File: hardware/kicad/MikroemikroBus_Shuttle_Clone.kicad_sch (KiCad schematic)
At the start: 3 parts, among them U28 X1270WV-2X08B-6TV01

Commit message: updating symbols to use kicad footprints where possible
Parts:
- C18, C19: footprint 5v rail sm-easyedapro:C0603 -> Capacitor_SMD:C_0603_1608Metric
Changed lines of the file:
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@@
 			)
 		)
-		(property "Footprint" "5v rail sm-easyedapro:C0603"
+		(property "Footprint" "Capacitor_SMD:C_0603_1608Metric"
 			(at 162.56 93.98 0)
 			(effects
@@
 			)
 		)
-		(property "Footprint" "5v rail sm-easyedapro:C0603"
+		(property "Footprint" "Capacitor_SMD:C_0603_1608Metric"
 			(at 107.95 93.98 0)
 			(effects

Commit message: update
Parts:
- renumbered C18 to C131, C19 to C133, U28 to U83
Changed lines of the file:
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@@
 		(dnp no)
 		(fields_autoplaced yes)
-		(property "Reference" "C19"
+		(property "Reference" "C133"
 			(at 166.37 93.9799 90)
 			(effects
@@
 				(path "/3f85abf4-0b95-4c4a-b7e9-06f59ca1ea3d/5c2e021f-c2d4-49e2-8c36-9a64f1f12001/1974f87f-12b5-4c85-8a00-765c6eb0fd1f"
 					(reference "C133")
-					(unit 1)
-				)
-				(path "/3f85abf4-0b95-4c4a-b7e9-06f59ca1ea3d/5c2e021f-c2d4-49e2-8c36-9a64f1f12001/83efc904-75ae-4d48-8a92-f421069b4636"
-					(reference "C19")
 					(unit 1)
 				)
@@
 		(on_board yes)
 		(dnp no)
-		(property "Reference" "#PWR075"
+		(property "Reference" "#PWR0170"
 			(at 162.56 104.14 0)
 			(effects
@@
 				(path "/3f85abf4-0b95-4c4a-b7e9-06f59ca1ea3d/5c2e021f-c2d4-49e2-8c36-9a64f1f12001/1974f87f-12b5-4c85-8a00-765c6eb0fd1f"
 					(reference "#PWR0170")
-					(unit 1)
-				)
-				(path "/3f85abf4-0b95-4c4a-b7e9-06f59ca1ea3d/5c2e021f-c2d4-49e2-8c36-9a64f1f12001/83efc904-75ae-4d48-8a92-f421069b4636"
-					(reference "#PWR075")
 					(unit 1)
 				)
@@
 		(on_board yes)
 		(dnp no)
-		(property "Reference" "#PWR072"
+		(property "Reference" "#PWR0167"
 			(at 107.95 104.14 0)
 			(effects
@@
 				(path "/3f85abf4-0b95-4c4a-b7e9-06f59ca1ea3d/5c2e021f-c2d4-49e2-8c36-9a64f1f12001/1974f87f-12b5-4c85-8a00-765c6eb0fd1f"
 					(reference "#PWR0167")
-					(unit 1)
-				)
-				(path "/3f85abf4-0b95-4c4a-b7e9-06f59ca1ea3d/5c2e021f-c2d4-49e2-8c36-9a64f1f12001/83efc904-75ae-4d48-8a92-f421069b4636"
-					(reference "#PWR072")
 					(unit 1)
 				)
@@
 		(dnp no)
 		(fields_autoplaced yes)
-		(property "Reference" "C18"
+		(property "Reference" "C131"
 			(at 111.76 93.9799 90)
 			(effects
@@
 				(path "/3f85abf4-0b95-4c4a-b7e9-06f59ca1ea3d/5c2e021f-c2d4-49e2-8c36-9a64f1f12001/1974f87f-12b5-4c85-8a00-765c6eb0fd1f"
 					(reference "C131")
-					(unit 1)
-				)
-				(path "/3f85abf4-0b95-4c4a-b7e9-06f59ca1ea3d/5c2e021f-c2d4-49e2-8c36-9a64f1f12001/83efc904-75ae-4d48-8a92-f421069b4636"
-					(reference "C18")
 					(unit 1)
 				)
@@
 		(on_board yes)
 		(dnp no)
-		(property "Reference" "#PWR074"
+		(property "Reference" "#PWR0169"
 			(at 151.13 106.68 0)
 			(effects
@@
 				(path "/3f85abf4-0b95-4c4a-b7e9-06f59ca1ea3d/5c2e021f-c2d4-49e2-8c36-9a64f1f12001/1974f87f-12b5-4c85-8a00-765c6eb0fd1f"
 					(reference "#PWR0169")
-					(unit 1)
-				)
-				(path "/3f85abf4-0b95-4c4a-b7e9-06f59ca1ea3d/5c2e021f-c2d4-49e2-8c36-9a64f1f12001/83efc904-75ae-4d48-8a92-f421069b4636"
-					(reference "#PWR074")
 					(unit 1)
 				)
@@
 		(on_board yes)
 		(dnp no)
-		(property "Reference" "#PWR073"
+		(property "Reference" "#PWR0168"
 			(at 121.92 104.14 0)
 			(effects
@@
 				(path "/3f85abf4-0b95-4c4a-b7e9-06f59ca1ea3d/5c2e021f-c2d4-49e2-8c36-9a64f1f12001/1974f87f-12b5-4c85-8a00-765c6eb0fd1f"
 					(reference "#PWR0168")
-					(unit 1)
-				)
-				(path "/3f85abf4-0b95-4c4a-b7e9-06f59ca1ea3d/5c2e021f-c2d4-49e2-8c36-9a64f1f12001/83efc904-75ae-4d48-8a92-f421069b4636"
-					(reference "#PWR073")
 					(unit 1)
 				)
@@
 		(on_board yes)
 		(dnp no)
-		(property "Reference" "U28"
+		(property "Reference" "U83"
 			(at 135.89 91.44 0)
 			(effects
@@
 					(unit 1)
 				)
-				(path "/3f85abf4-0b95-4c4a-b7e9-06f59ca1ea3d/5c2e021f-c2d4-49e2-8c36-9a64f1f12001/83efc904-75ae-4d48-8a92-f421069b4636"
-					(reference "U28")
-					(unit 1)
-				)

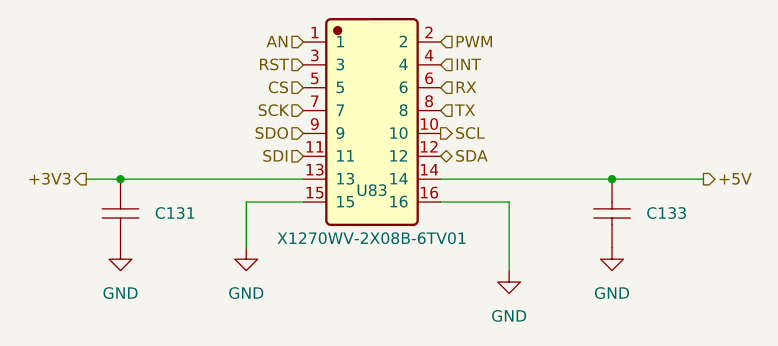
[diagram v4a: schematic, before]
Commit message: fixing inconsistencies in value convention
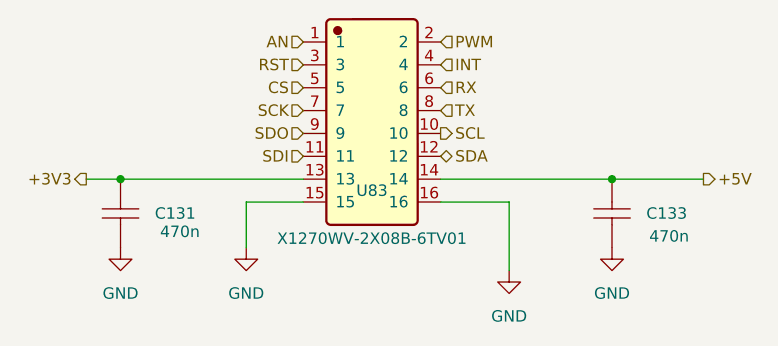
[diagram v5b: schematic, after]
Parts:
- C131, C133: value 470nF -> 470n
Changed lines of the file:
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@@
 		(on_board yes)
 		(dnp no)
-		(fields_autoplaced yes)
 		(property "Reference" "C133"
 			(at 166.37 93.9799 90)
@@
 			)
 		)
-		(property "Value" "470nF"
-			(at 162.56 93.98 0)
-			(effects
-				(font
-					(size 1.27 1.27)
-				)
-				(hide yes)
+		(property "Value" "470n"
+			(at 168.91 96.52 90)
+			(effects
+				(font
+					(size 1.27 1.27)
+				)
 			)
 		)
@@
 		(on_board yes)
 		(dnp no)
-		(fields_autoplaced yes)
 		(property "Reference" "C131"
 			(at 111.76 93.9799 90)
@@
 			)
 		)
-		(property "Value" "470nF"
-			(at 107.95 93.98 0)
-			(effects
-				(font
-					(size 1.27 1.27)
-				)
-				(hide yes)
-			)
-		)
+		(property "Value" "470n"
+			(at 114.554 96.012 90)
+			(effects
+				(font
+					(size 1.27 1.27)
+				)
+			)
+		)

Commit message: improved margins for shuttle connector
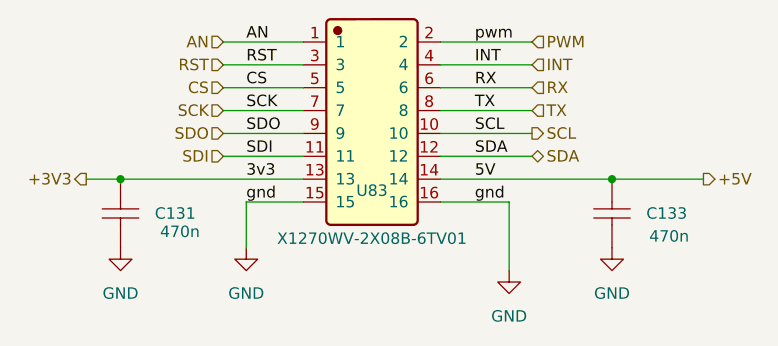
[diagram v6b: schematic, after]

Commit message: exported to schematic
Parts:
- C131, C133: LCSC (none) -> C77572
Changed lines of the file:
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@@
+			)
+		)
+		(property "LCSC" "C77572"
+			(at 166.37 93.9799 0)
+			(effects
+				(font
+					(size 1.27 1.27)
+				)
+				(hide yes)
 			)
 		)
@@
 			(effects
 				(font
+					(size 1.27 1.27)
+				)
+				(hide yes)
+			)
+		)
+		(property "LCSC" "C77572"
+			(at 111.76 93.9799 0)
+			(effects
+				(font
